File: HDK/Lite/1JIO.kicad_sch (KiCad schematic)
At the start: 14 parts, among them J301 A1-SEL, J302 SSR, J303 CAN, J304 ANA, J305 PWR, J306 DIO, U301 KAQY214

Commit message: updated 1 Job
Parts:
- added C106: 100n, Capacitor_SMD:C_0603_1608Metric, symbol Device:C
- added D401, D402: B5819W, Diode_SMD:D_SOD-123, symbol Device:D_Schottky
- added J101: USB C, Connector_USB:USB_C_Receptacle_HRO_TYPE-C-31-M-12, symbol Connector:USB_C_Receptacle_USB2.0
- added R103, R104: 5.1k, Resistor_SMD:R_0603_1608Metric, symbol Device:R
- added U104: CH340N, Package_SO:SOIC-8_3.9x4.9mm_P1.27mm, symbol Interface_USB:CH330N
- renumbered J302 to J401, J303 to J402, J304 to J403, J305 to J404, J306 to J405, J301 to J406, R301 to R401, R302 to R402, R303 to R403, R304 to R404, R305 to R405, R306 to R406, R307 to R407, U301 to U401
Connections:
- net +3V3: now also C106.1, U104.5 (VCC)
- net GND: now also C106.2, J101.A1 (GND), J101.A12 (GND), J101.B1 (GND), J101.B12 (GND), R103.2, R104.2, U104.3 (GND)
- net +12V: no longer names the net of J404.1 (Pin_1)
- net +12V: now also D401.2 (A)
- new net: J101.A5 (CC1), R103.1
- new net: J101.B5 (CC2), R104.1
- new net SWCLK: J101.A8 (SBU1)
- new net SWDIO: J101.B8 (SBU2)
- new net UART1_RX: U104.7 (RXD)
- new net UART1_TX: U104.6 (TXD)
- new net USB_D+: J101.A6 (D+), J101.B6 (D+), U104.1 (UD+)
- new net USB_D-: J101.A7 (D-), J101.B7 (D-), U104.2 (UD-)
- new net VBUS: D402.2 (A), J101.A4 (VBUS), J101.A9 (VBUS), J101.B4 (VBUS), J101.B9 (VBUS)
- new net VCC: D401.1 (K), D402.1 (K)
- no-connect marks 0 -> 3
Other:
- note added: "USB C V_{max} = 5V"
- moved on the sheet: J401, J402, J403, J404, J405, J406, R401, R402, R403, R404, R405, R406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

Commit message: updated 1 Job, WIP
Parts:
- J401, J402, J404: footprint Connector_JST:JST_XH_B2B-XH-AM_1x02_P2.50mm_Vertical -> Connector_JST:JST_PH_S2B-PH-K_1x02_P2.00mm_Horizontal
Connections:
- net A1_DIV-05V: now also R404.1; no longer R404.2, R406.2
- net ANA_1: now also J406.1 (Pin_1), R404.2, R406.2; no longer J406.2 (Pin_2)
- net CAN_H: now also J402.2 (Pin_2); no longer J402.1 (Pin_1)
- net CAN_L: now also J402.1 (Pin_1); no longer J402.2 (Pin_2)
- net SSR-IN: now also U401.3; no longer U401.4
- net SSR-OUT: now also U401.4; no longer U401.3
- net A1_DIV-03V renamed A1_DIV-12V
- net A1_DIV-12V: now also J406.2 (Pin_2); no longer J406.1 (Pin_1), R404.1
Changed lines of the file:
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@@
     (stroke (width 0) (type default))
   )
-  (wire (pts (xy 44.45 74.93) (xy 68.58 74.93))
+  (wire (pts (xy 55.88 74.93) (xy 68.58 74.93))
     (stroke (width 0) (type default))
   )
@@
     (stroke (width 0) (type default))
   )
-  (wire (pts (xy 44.45 69.85) (xy 68.58 69.85))
+  (wire (pts (xy 55.88 69.85) (xy 68.58 69.85))
     (stroke (width 0) (type default))
   )
@@
     (effects (font (size 1.27 1.27)) (justify left bottom))
   )
+  (label "A1_DIV-03V" (at 44.45 63.5 0) (fields_autoplaced)
+    (effects (font (size 1.27 1.27)) (justify left bottom))
+  )
+  (label "ANA_1-IN" (at 44.45 72.39 0) (fields_autoplaced)
+    (effects (font (size 1.27 1.27)) (justify left bottom))
+  )
+  (label "A1_DIV-05V" (at 55.88 74.93 0) (fields_autoplaced)
+    (effects (font (size 1.27 1.27)) (justify left bottom))
+  )
   (label "ANA_1-IN" (at 172.72 60.96 0) (fields_autoplaced)
     (effects (font (size 1.27 1.27)) (justify left bottom))
@@
     (effects (font (size 1.27 1.27)) (justify left bottom))
   )
-  (label "A1_DIV-12V" (at 107.95 45.72 180) (fields_autoplaced)
-    (effects (font (size 1.27 1.27)) (justify right bottom))
-  )
-  (label "A1_DIV-05V" (at 44.45 74.93 0) (fields_autoplaced)
-    (effects (font (size 1.27 1.27)) (justify left bottom))
-  )
-  (label "A1_DIV-03V" (at 107.95 63.5 180) (fields_autoplaced)
-    (effects (font (size 1.27 1.27)) (justify right bottom))
-  )
-  (label "SSR-IN" (at 95.25 93.98 180) (fields_autoplaced)
+  (label "SSR-IN" (at 95.25 99.06 180) (fields_autoplaced)
     (effects (font (size 1.27 1.27)) (justify right bottom))
   )
@@
     (effects (font (size 1.27 1.27)) (justify left bottom))
   )
-  (label "A1_DIV-03V" (at 44.45 69.85 0) (fields_autoplaced)
+  (label "A1_DIV-05V" (at 44.45 53.34 0) (fields_autoplaced)
     (effects (font (size 1.27 1.27)) (justify left bottom))
   )
@@
     (effects (font (size 1.27 1.27)) (justify left bottom))
   )
-  (label "CAN_H" (at 240.03 50.8 180) (fields_autoplaced)
+  (label "CAN_H" (at 240.03 53.34 180) (fields_autoplaced)
     (effects (font (size 1.27 1.27)) (justify right bottom))
   )
@@
     (effects (font (size 1.27 1.27)) (justify left bottom))
   )
-  (label "ANA_1" (at 59.69 72.39 0) (fields_autoplaced)
-    (effects (font (size 1.27 1.27)) (justify left bottom))
-  )
-  (label "A1_DIV-05V" (at 107.95 55.88 180) (fields_autoplaced)
-    (effects (font (size 1.27 1.27)) (justify right bottom))
-  )
-  (label "SSR-OUT" (at 95.25 99.06 180) (fields_autoplaced)
+  (label "A1_DIV-12V" (at 44.45 43.18 0) (fields_autoplaced)
+    (effects (font (size 1.27 1.27)) (justify left bottom))
+  )
+  (label "SSR-OUT" (at 95.25 93.98 180) (fields_autoplaced)
     (effects (font (size 1.27 1.27)) (justify right bottom))
   )
@@
     (effects (font (size 1.27 1.27)) (justify right bottom))
   )
-  (label "A1_DIV-12V" (at 44.45 72.39 0) (fields_autoplaced)
-    (effects (font (size 1.27 1.27)) (justify left bottom))
-  )
-  (label "ANA_1-IN" (at 44.45 63.5 0) (fields_autoplaced)
-    (effects (font (size 1.27 1.27)) (justify left bottom))
-  )
-  (label "ANA_1-IN" (at 44.45 43.18 0) (fields_autoplaced)
+  (label "A1_DIV-03V" (at 55.88 69.85 0) (fields_autoplaced)
     (effects (font (size 1.27 1.27)) (justify left bottom))
   )
@@
     (effects (font (size 1.27 1.27)) (justify left bottom))
   )
-  (label "CAN_L" (at 240.03 53.34 180) (fields_autoplaced)
+  (label "A1_DIV-12V" (at 55.88 72.39 0) (fields_autoplaced)
+    (effects (font (size 1.27 1.27)) (justify left bottom))
+  )
+  (label "CAN_L" (at 240.03 50.8 180) (fields_autoplaced)
     (effects (font (size 1.27 1.27)) (justify right bottom))
   )
-  (label "ANA_1-IN" (at 44.45 53.34 0) (fields_autoplaced)
-    (effects (font (size 1.27 1.27)) (justify left bottom))
-  )
-  (hierarchical_label "ANA_1" (shape input) (at 44.45 72.39 180) (fields_autoplaced)
-    (effects (font (size 1.27 1.27)) (justify right))
+  (hierarchical_label "ANA_1" (shape input) (at 107.95 55.88 0) (fields_autoplaced)
+    (effects (font (size 1.27 1.27)) (justify left))
+  )
+  (hierarchical_label "ANA_1" (shape input) (at 107.95 45.72 0) (fields_autoplaced)
+    (effects (font (size 1.27 1.27)) (justify left))
   )
   (hierarchical_label "DO_SSR" (shape input) (at 44.45 93.98 180) (fields_autoplaced)
     (effects (font (size 1.27 1.27)) (justify right))
   )
-  (hierarchical_label "CAN_L" (shape input) (at 240.03 53.34 0) (fields_autoplaced)
+  (hierarchical_label "CAN_L" (shape input) (at 240.03 50.8 0) (fields_autoplaced)
     (effects (font (size 1.27 1.27)) (justify left))
   )
@@
     (effects (font (size 1.27 1.27)) (justify left))
   )
-  (hierarchical_label "CAN_H" (shape input) (at 240.03 50.8 0) (fields_autoplaced)
+  (hierarchical_label "ANA_1" (shape input) (at 107.95 63.5 0) (fields_autoplaced)
+    (effects (font (size 1.27 1.27)) (justify left))
+  )
+  (hierarchical_label "CAN_H" (shape input) (at 240.03 53.34 0) (fields_autoplaced)
     (effects (font (size 1.27 1.27)) (justify left))
   )
@@
       (effects (font (size 1.27 1.27)) (justify left))
     )
-    (property "Footprint" "Connector_JST:JST_XH_B2B-XH-AM_1x02_P2.50mm_Vertical" (at 189.23 50.8 0)
+    (property "Footprint" "Connector_JST:JST_PH_S2B-PH-K_1x02_P2.00mm_Horizontal" (at 189.23 50.8 0)
       (effects (font (size 1.27 1.27)) hide)
     )
@@
       (effects (font (size 1.27 1.27)) (justify left))
     )
-    (property "Footprint" "Connector_JST:JST_XH_B2B-XH-AM_1x02_P2.50mm_Vertical" (at 223.52 50.8 0)
+    (property "Footprint" "Connector_JST:JST_PH_S2B-PH-K_1x02_P2.00mm_Horizontal" (at 223.52 50.8 0)
       (effects (font (size 1.27 1.27)) hide)
     )
@@
       (effects (font (size 1.27 1.27)) (justify left))
     )
-    (property "Footprint" "Connector_JST:JST_XH_B2B-XH-AM_1x02_P2.50mm_Vertical" (at 223.52 69.85 0)
-      (effects (font (size 1.27 1.27)) hide)
-    )
+    (property "Footprint" "Connector_JST:JST_PH_S2B-PH-K_1x02_P2.00mm_Horizontal" (at 223.52 69.85 0)
+      (effects (font (size 1.27 1.27)) hide)
+    )

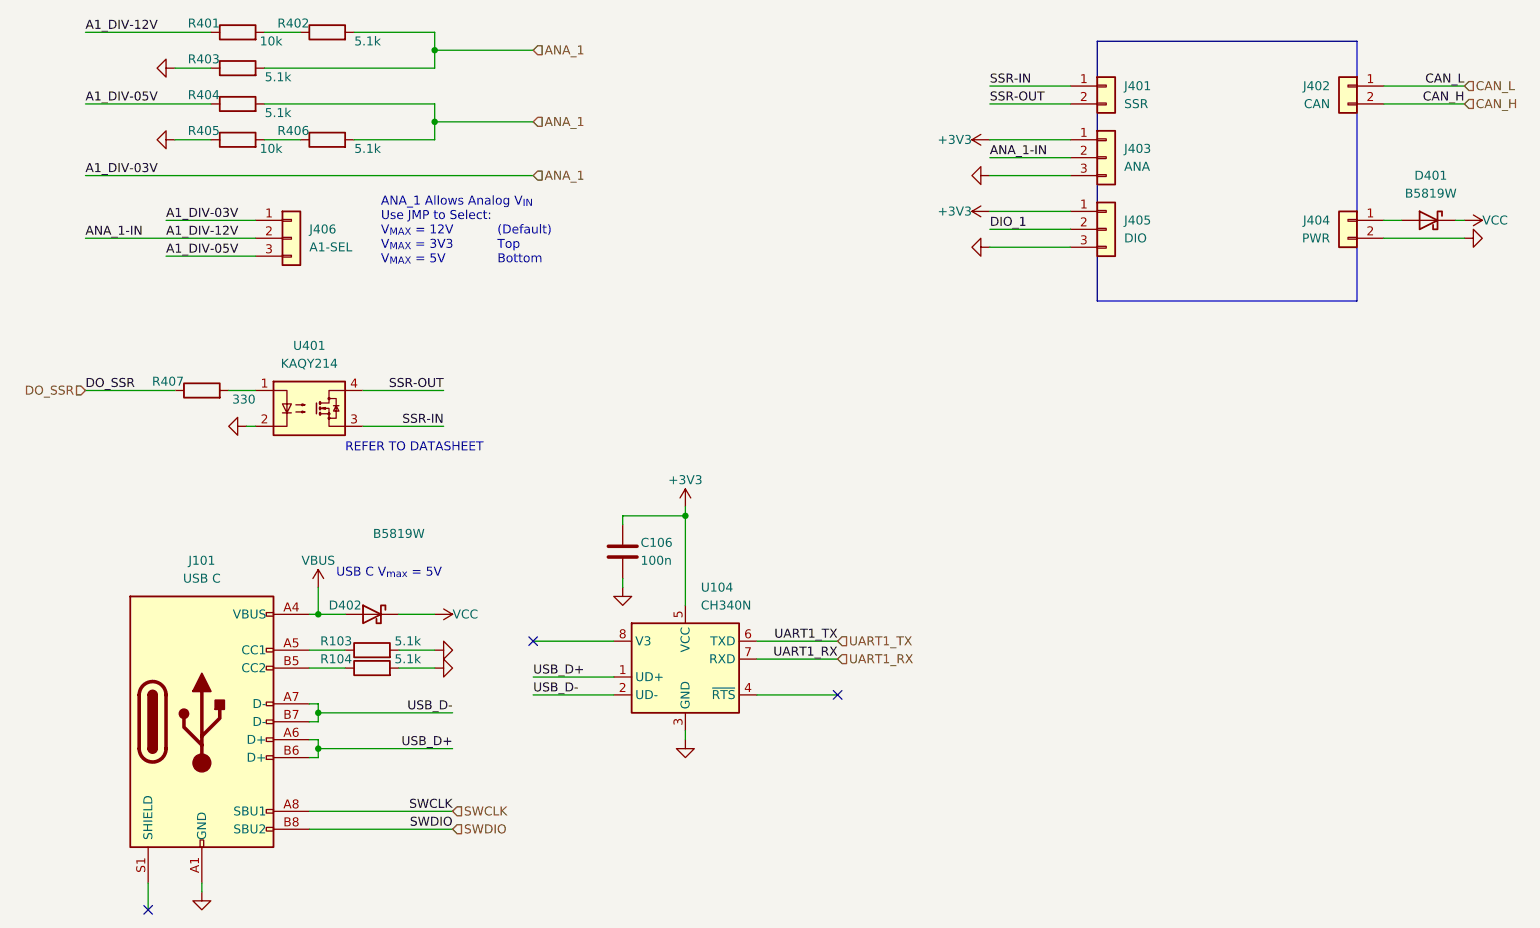
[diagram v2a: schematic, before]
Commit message: updated 1Job, 75%
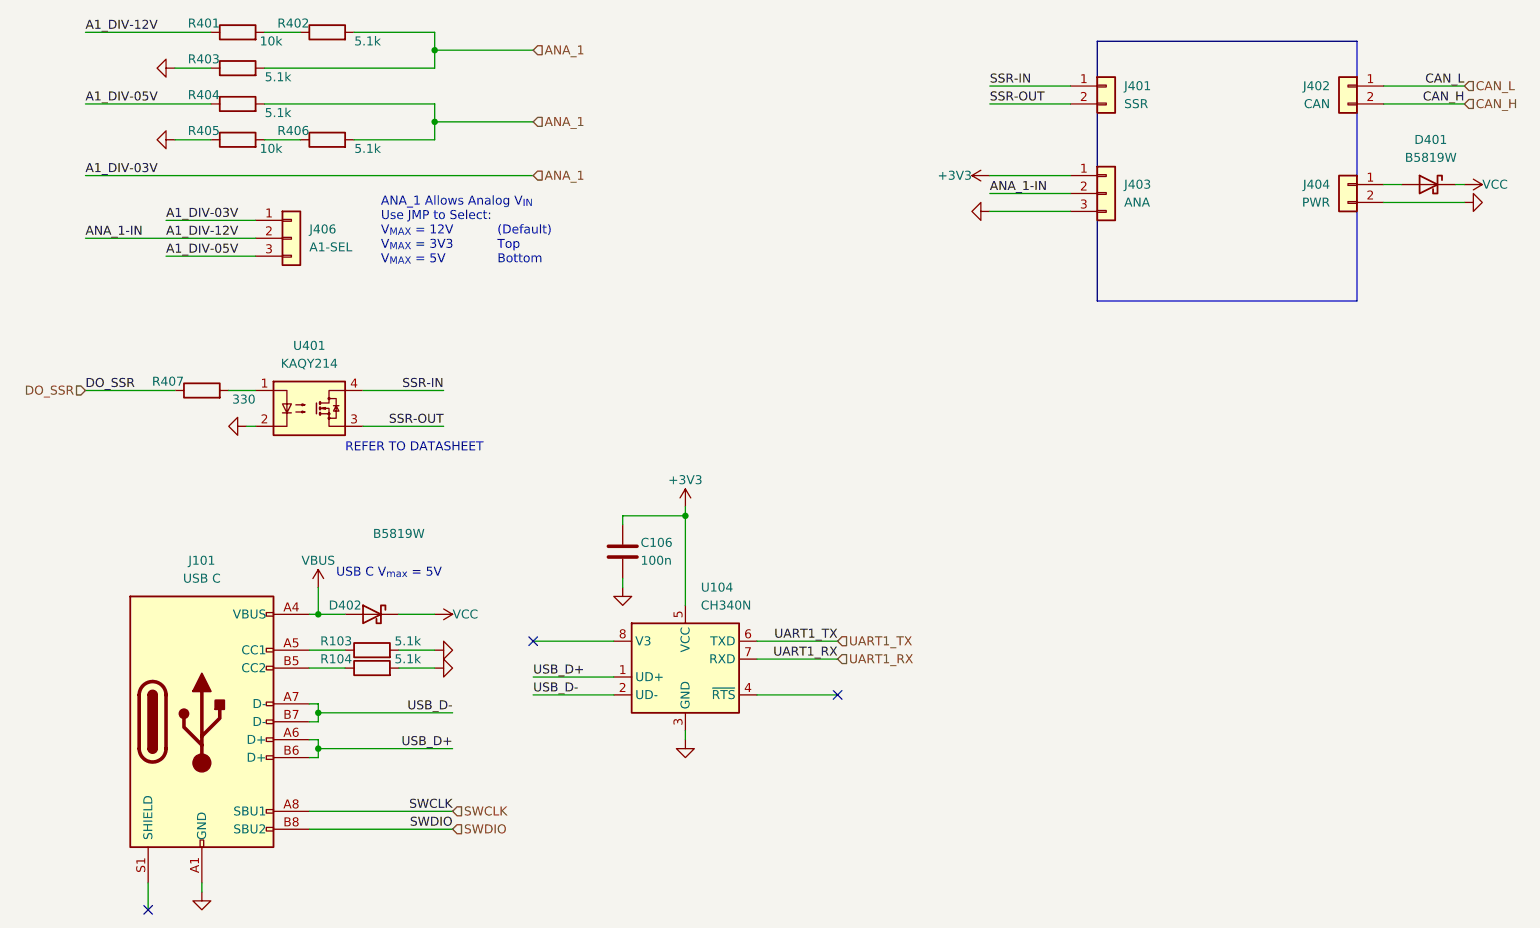
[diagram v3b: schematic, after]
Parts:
- removed J405: DIO, Connector_JST:JST_PH_S3B-PH-K_1x03_P2.00mm_Horizontal, symbol Connector_Generic:Conn_01x03
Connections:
- net SSR-IN: now also U401.4; no longer U401.3
- net SSR-OUT: now also U401.3; no longer U401.4
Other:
- moved on the sheet: D401, J403, J404

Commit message: updated 1 Job, 85%
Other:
- moved on the sheet: D401, J401, J402, J403, J404

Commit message: updated 1-Job, v1rA
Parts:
- added J405: Conn_02x14_Odd_Even, NVF-Kicad:48x48 Module, symbol Connector_Generic:Conn_02x14_Odd_Even
- C106: LCSC (none) -> C57112
- J101: footprint Connector_USB:USB_C_Receptacle_HRO_TYPE-C-31-M-12 -> NVF-Kicad:USB_C_Receptacle_HRO_TYPE-C-31-M-12; LCSC (none) -> C165948
- J401, J402, J404: footprint Connector_JST:JST_PH_S2B-PH-K_1x02_P2.00mm_Horizontal -> NVF-Kicad:JST-PH-1x02-Horizontal; LCSC (none) -> C173752
- J403: footprint Connector_JST:JST_PH_S3B-PH-K_1x03_P2.00mm_Horizontal -> NVF-Kicad:JST-PH-1x03-Horizontal; LCSC (none) -> C157929
- J406: footprint Connector_PinHeader_2.54mm:PinHeader_1x03_P2.54mm_Vertical -> Connector_PinHeader_2.54mm:PinHeader_1x03_P2.54mm_Horizontal
- R103, R104, R402, R403, R404, R406: LCSC (none) -> 0603
- R401, R405: LCSC (none) -> C25804
- R407: LCSC (none) -> C23138
- U104: LCSC (none) -> C2977777
- U401: LCSC (none) -> C113331
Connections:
- net +3V3: now also J405.1 (Pin_1), J405.24 (Pin_24)
- net GND: now also J405.2 (Pin_2), J405.25 (Pin_25), J405.26 (Pin_26)
- net SSR-IN: now also J401.2 (Pin_2); no longer J401.1 (Pin_1)
- net SSR-OUT: now also J401.1 (Pin_1); no longer J401.2 (Pin_2)
- net SWCLK: now also J405.22 (Pin_22)
- net SWDIO: now also J405.20 (Pin_20)
- net UART1_RX: now also J405.23 (Pin_23)
- net UART1_TX: now also J405.21 (Pin_21)
- net VCC: now also J405.28 (Pin_28)
- new net I2C1_SCL: J405.9 (Pin_9)
- new net I2C1_SDA: J405.7 (Pin_7)
- new net I2C2_SCL: J405.11 (Pin_11)
- new net I2C2_SDA: J405.13 (Pin_13)
- new net PB3: J405.15 (Pin_15)
- new net PB4: J405.17 (Pin_17)
- new net PB5: J405.19 (Pin_19)
- new net SPI1_MISO: J405.10 (Pin_10)
- new net SPI1_MOSI: J405.12 (Pin_12)
- new net SPI1_SCK: J405.8 (Pin_8)
- new net SPI2_MISO: J405.16 (Pin_16)
- new net SPI2_MOSI: J405.18 (Pin_18)
- new net SPI2_SCK: J405.14 (Pin_14)
- new net UART2_RX: J405.4 (Pin_4)
- new net UART2_TX: J405.6 (Pin_6)
- new net ~{NRST}: J405.27 (Pin_27)

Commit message: updated 1job
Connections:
- no-connect marks 3 -> 5
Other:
- company: (none) -> Scott CJX
- title: (none) -> 1 Job Lite
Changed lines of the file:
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@@
 (kicad_sch (version 20230121) (generator eeschema)
   (paper "A4")
+  (title_block
+    (title "1 Job Lite")
+    (date "2023-11-13")
+    (rev "A")
+    (company "Scott CJX")
+  )
   (junction (at 77.47 144.78) (diameter 0) (color 0 0 0 0)
   )
@@
   (no_connect (at 107.95 129.54))
   (no_connect (at 53.34 167.64))
+  (no_connect (at 186.69 105.41))
   (no_connect (at 151.13 137.16))
+  (no_connect (at 186.69 102.87))
   (wire (pts (xy 77.47 121.92) (xy 77.47 125.73))
     (stroke (width 0) (type default))
